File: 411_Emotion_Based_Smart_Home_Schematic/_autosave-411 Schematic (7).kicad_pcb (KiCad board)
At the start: 2 copper layers, 123 x 48 mm, 25 parts, among them Q1 NSS1C301ET4G, Q2 NSS1C301ET4G, Q3 NSS1C301ET4G, U4 HC-SR04

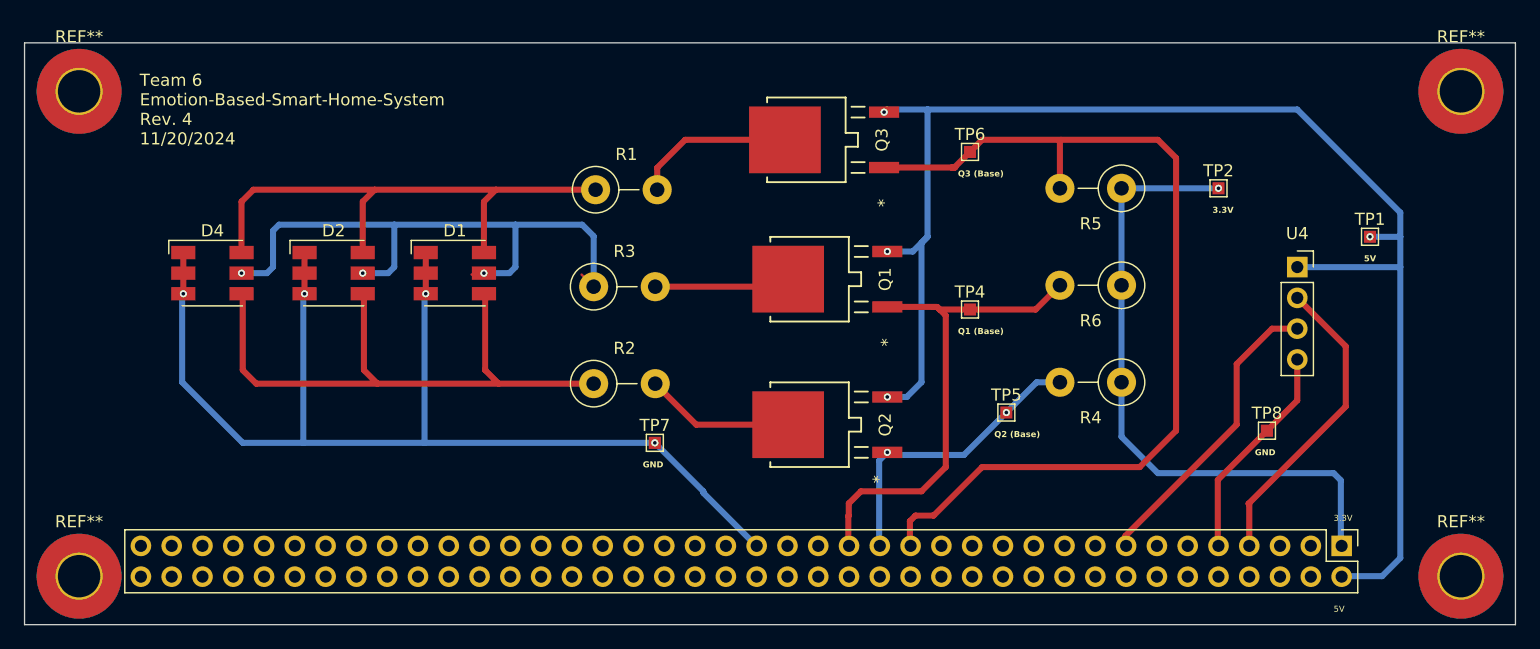
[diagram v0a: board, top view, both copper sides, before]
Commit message: Updated schematic.
Added limiting resistors to each GPIO pins.
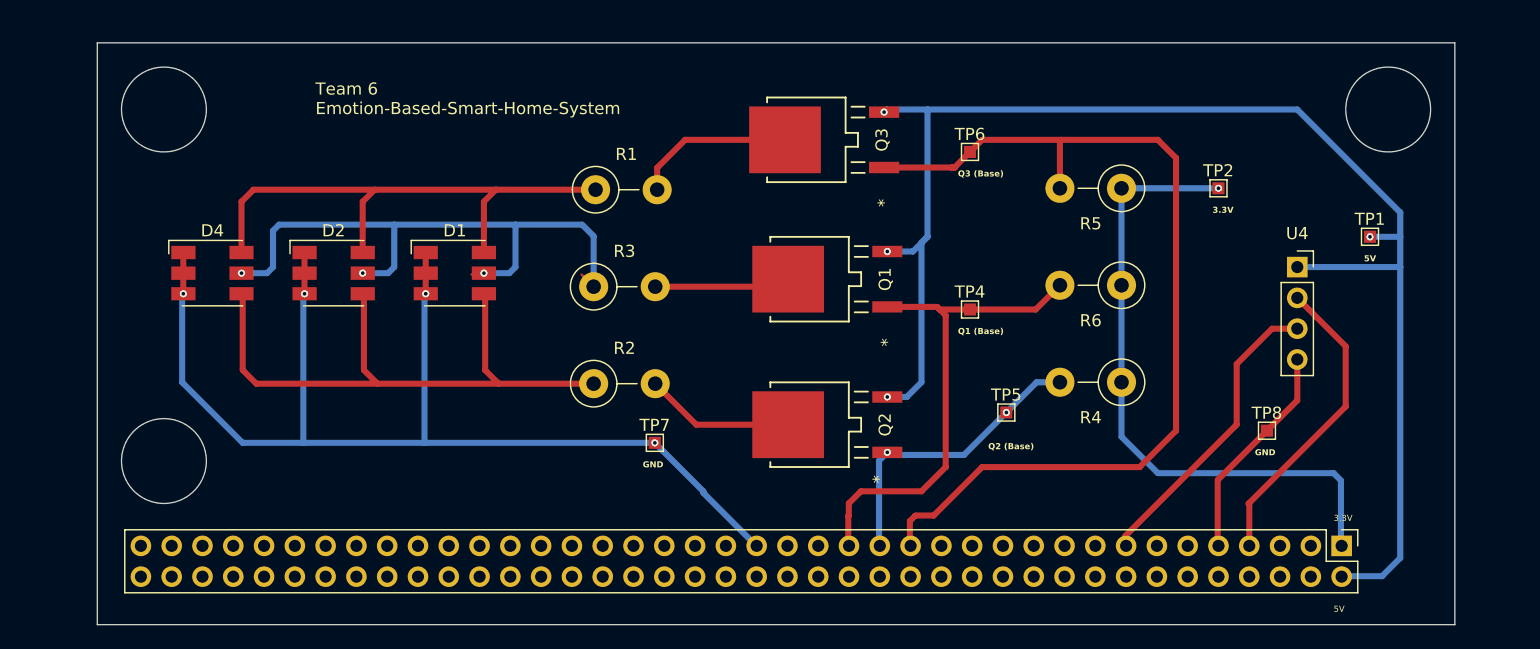
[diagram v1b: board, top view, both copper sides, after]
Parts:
- removed REF** (x4): MountingHole_3.5mm_Pad_TopBottom, MountingHole:MountingHole_3.5mm_Pad_TopBottom
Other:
- board size 123 x 48 mm -> 112 x 48 mm
- board text added: "Team 6 Emotion-Based-Smart-Home-System"
- board text removed: "Team 6 Emotion-Based-Smart-Home-System Rev. 4 11/20/2024"
